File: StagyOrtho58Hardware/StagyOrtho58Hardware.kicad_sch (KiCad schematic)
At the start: 72 parts, among them J11 USB_C_Receptacle, SW11 SW_Push, SW12 SW_Push, SW13 SW_Push, SW14 SW_Push, SW15 SW_Push, SW16 SW_Push, SW17 SW_Push, SW18 SW_Push, SW19 SW_Push, SW20 SW_Push, SW21 SW_Push, SW22 SW_Push, SW23 SW_Push, SW24 SW_Push, SW25 SW_Push, SW26 SW_Push, SW27 SW_Push, SW28 SW_Push, SW29 SW_Push, SW30 SW_Push, SW31 SW_Push, SW32 SW_Push, SW33 SW_Push, SW34 SW_Push, SW35 SW_Push, SW36 SW_Push, SW37 SW_Push, SW38 SW_Push, SW39 SW_Push, SW40 SW_Push, U11 Pico, U12 MCP23S17_ML

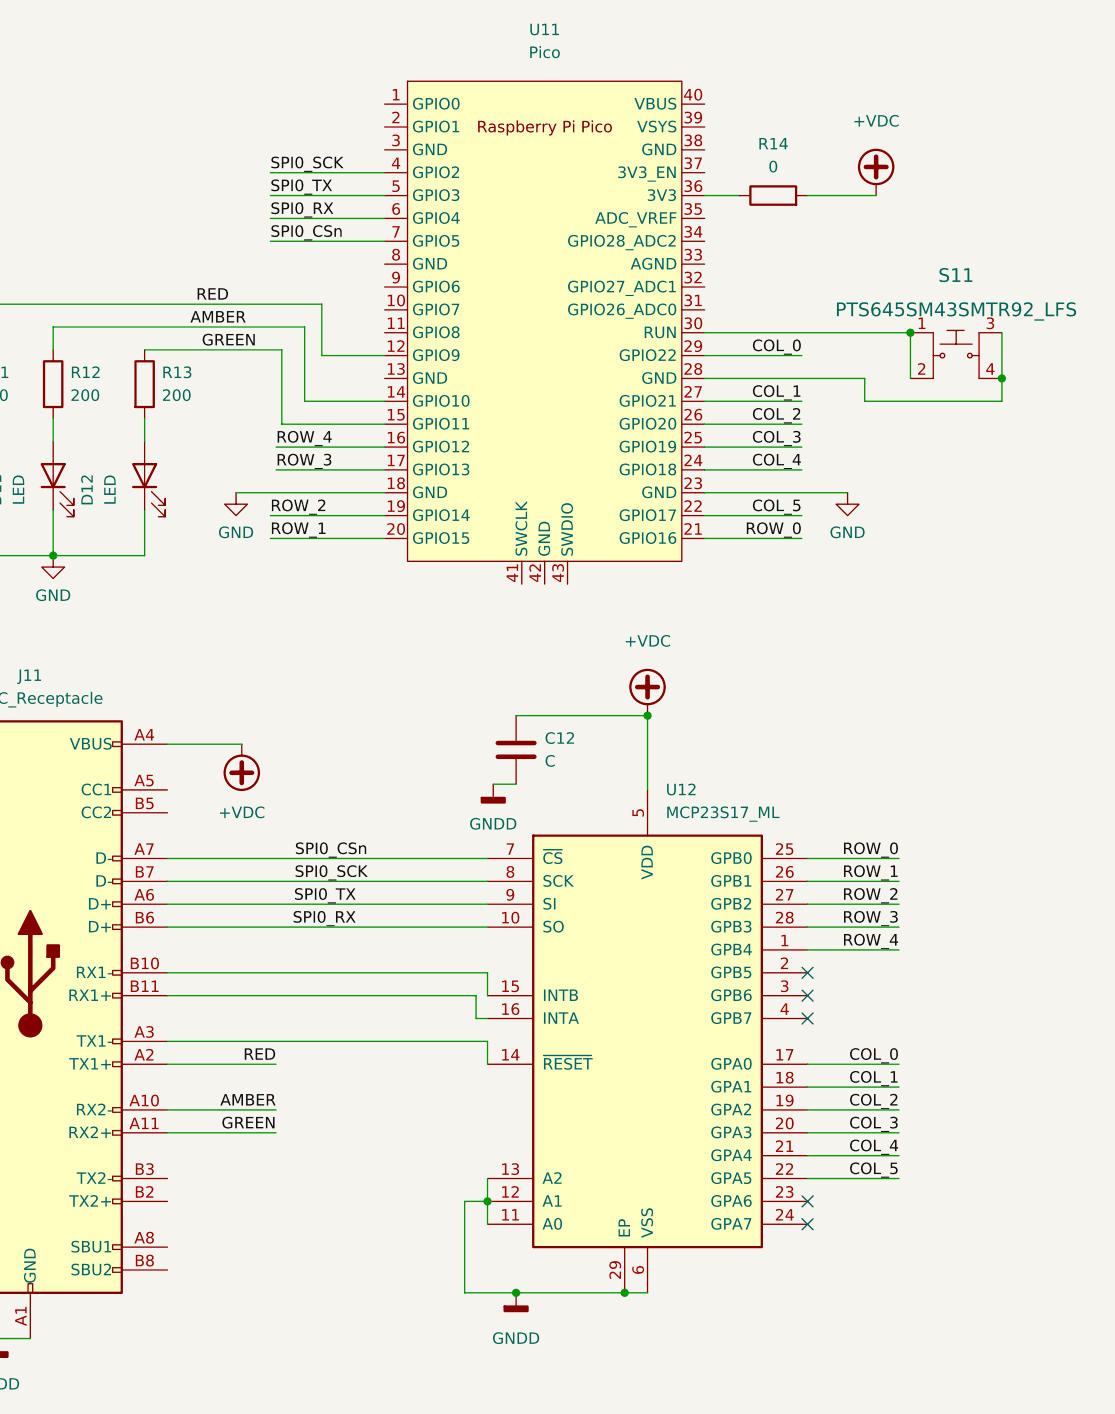
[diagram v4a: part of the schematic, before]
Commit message: Working draft for key positions
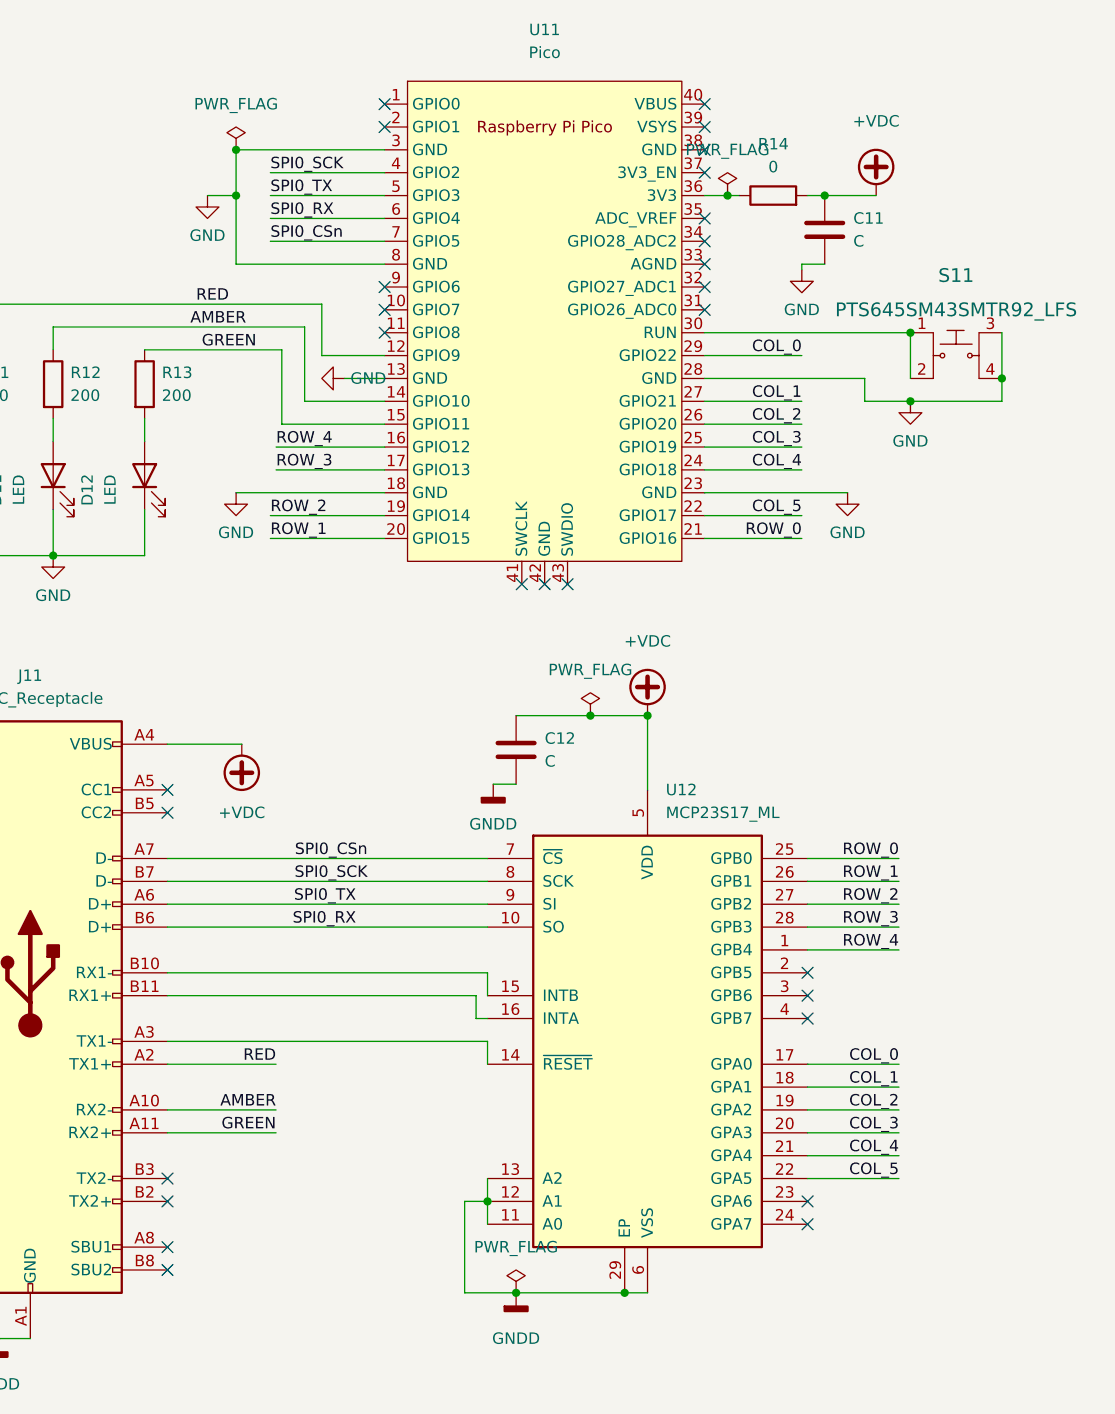
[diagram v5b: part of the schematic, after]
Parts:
- added C11: C, Capacitor_SMD:C_0603_1608Metric, symbol Device:C
- J11: footprint (none) -> Connector_USB:USB_C_Receptacle_GCT_USB4085
- SW11, SW40: footprint (none) -> Switch_Keyboard_Kailh:SW_Kailh_Choc_V1V2_1.00u
- SW17, SW23, SW29: footprint (none) -> Switch_Keyboard_Kailh:SW_Kailh_Choc_V1V2_1.50u
- SW35, SW37: footprint Switch_Keyboard_Kailh:SW_Kailh_Choc_V1V2_1.25u -> Switch_Keyboard_Kailh:SW_Kailh_Choc_V1V2_1.50u
- SW36: footprint Switch_Keyboard_Kailh:SW_Kailh_Choc_V1V2_1.25u -> Switch_Keyboard_Kailh:SW_Kailh_Choc_V1V2_1.00u
- SW38: footprint (none) -> Switch_Keyboard_Kailh:SW_Kailh_Choc_V1V2_1.50u_90deg
- SW39: footprint (none) -> Switch_Keyboard_Kailh:SW_Kailh_Choc_V1V2_2.00u
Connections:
- net +VDC: now also C11.1
- net GND: now also S11.3, S11.4, U11.13 (GND), U11.28 (GND), U11.3 (GND), U11.8 (GND), C11.2
- no-connect marks 5 -> 28

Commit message: Comfortable positions of the keys, ready to layout
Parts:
- removed J11: USB_C_Receptacle, Connector_USB:USB_C_Receptacle_GCT_USB4085, symbol Connector:USB_C_Receptacle
- added J11: USB_C_Receptacle_USB2.0, Connector_USB:USB_C_Receptacle_GCT_USB4085, symbol Connector:USB_C_Receptacle_USB2.0
- SW29: footprint Switch_Keyboard_Kailh:SW_Kailh_Choc_V1V2_1.50u -> Switch_Keyboard_Kailh:SW_Kailh_Choc_V1V2_2.00u
- SW35, SW37: footprint Switch_Keyboard_Kailh:SW_Kailh_Choc_V1V2_1.50u -> Switch_Keyboard_Kailh:SW_Kailh_Choc_V1V2_1.00u
- SW38: footprint Switch_Keyboard_Kailh:SW_Kailh_Choc_V1V2_1.50u_90deg -> Switch_Keyboard_Kailh:SW_Kailh_Choc_V1V2_1.00u
- SW39: footprint Switch_Keyboard_Kailh:SW_Kailh_Choc_V1V2_2.00u -> Switch_Keyboard_Kailh:SW_Kailh_Choc_V1V2_1.00u
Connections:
- net +VDC: now also J11.A4 (VBUS), J11.A9 (VBUS), J11.B4 (VBUS), J11.B9 (VBUS)
- net GNDD: now also J11.A1 (GND), J11.A12 (GND), J11.B1 (GND), J11.B12 (GND), J11.S1 (SHIELD)
- net GREEN: now also J11.B5 (CC2)
- net SPI0_CSn: now also J11.A7 (D-)
- net SPI0_RX: now also J11.B6 (D+)
- net SPI0_SCK: now also J11.B7 (D-)
- net SPI0_TX: now also J11.A6 (D+)
- net ~{RESET}: now reaches U12.14 (~{RESET})
- net ~{RESET}: now also J11.A5 (CC1)
- net at U12.15 (INTB): now also J11.A8 (SBU1)
- net at U12.16 (INTA): now also J11.B8 (SBU2)
- no-connect marks 28 -> 22

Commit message: Placed all components, board outline added
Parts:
- U11: footprint MCU_RaspberryPi_and_Boards:RPi_Pico_SMD_TH -> RPi_Pico:RPi_Pico_SMD_TH
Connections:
- net INTB: now reaches J11.A8 (SBU1), U12.15 (INTB)
- net INTA: now reaches J11.B8 (SBU2), U12.16 (INTA)
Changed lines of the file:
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@@
     (effects (font (size 1.27 1.27)) (justify right bottom))
+  )
+  (label "INTA" (at 200.025 129.54 0)
+    (effects (font (size 1.27 1.27)) (justify left bottom))
   )
   (label "COL_2" (at 252.73 63.5 180)
@@
   (label "COL_3" (at 252.73 66.04 180)
     (effects (font (size 1.27 1.27)) (justify right bottom))
+  )
+  (label "INTB" (at 200.025 127 0)
+    (effects (font (size 1.27 1.27)) (justify left bottom))
   )
   (label "SPI0_TX" (at 203.2 116.84 180)
@@
     (property "Reference" "U11" (id 0) (at 224.155 19.685 0))
     (property "Value" "Pico" (id 1) (at 224.155 22.225 0))
-    (property "Footprint" "MCU_RaspberryPi_and_Boards:RPi_Pico_SMD_TH" (id 2) (at 224.155 52.07 90)
+    (property "Footprint" "RPi_Pico:RPi_Pico_SMD_TH" (id 2) (at 224.155 52.07 90)
       (effects (font (size 1.27 1.27)) hide)
     )
@@
     )
     (path "/33cc3892-3d60-443c-a486-cdd4054d3053"
-      (reference "U11") (unit 1) (value "Pico") (footprint "MCU_RaspberryPi_and_Boards:RPi_Pico_SMD_TH")
+      (reference "U11") (unit 1) (value "Pico") (footprint "RPi_Pico:RPi_Pico_SMD_TH")
     )
     (path "/dd1b4e60-76de-468d-8e52-6436cad5e7c0"

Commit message: Partial routing complete, approx 40%
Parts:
- added H11, H12, H13, H14, H15, H16: MountingHole, MountingHole:MountingHole_3.2mm_M3, symbol Mechanical:MountingHole
- added H17, H18, H19, H20: MountingHole, MountingHole:MountingHole_2.7mm_M2.5, symbol Mechanical:MountingHole
- SW37: footprint Switch_Keyboard_Kailh:SW_Kailh_Choc_V1V2_1.00u -> Switch_Keyboard_Kailh:SW_Kailh_Choc_V1V2_1.50u
